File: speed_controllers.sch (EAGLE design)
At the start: 31 parts, among them M1 TE-1-1123723-3, M2 TE-1-1123723-3, M3 TE-1-1123723-3, M4 TE-1-1123723-3, M5 TE-1-1123723-3, M6 TE-1-1123723-3, M7 TE-1-1123723-3, M8 TE-1-1123723-3

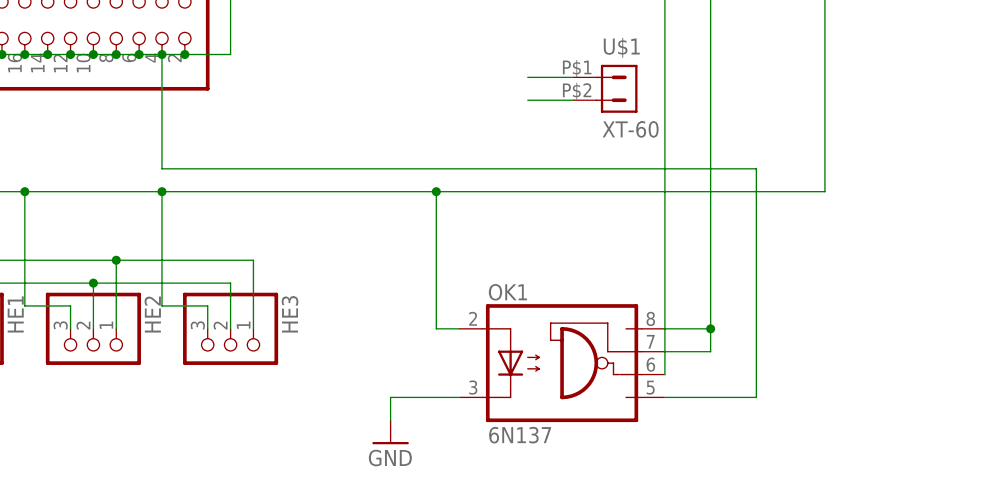
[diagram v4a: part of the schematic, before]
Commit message: Changed optocoupler to SMD
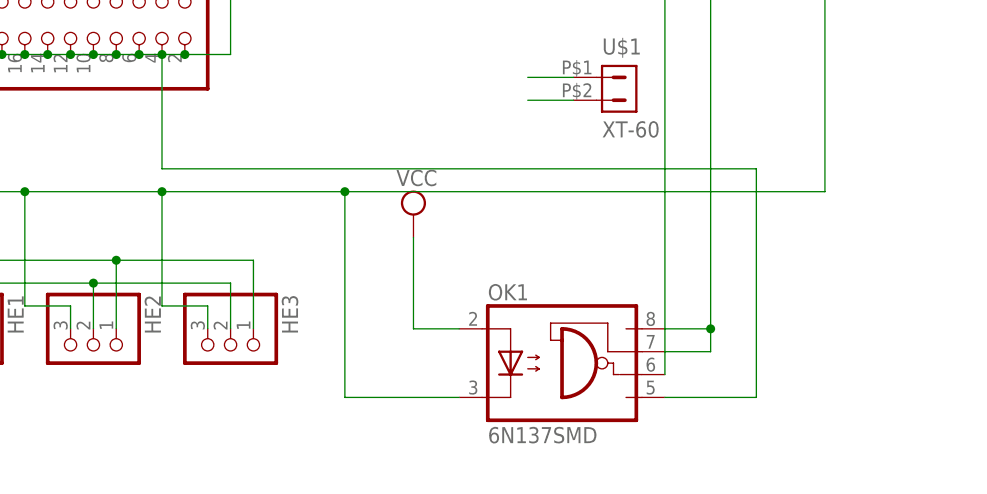
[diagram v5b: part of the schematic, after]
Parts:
- OK1: value 6N137 -> 6N137SMD; device auv:6N137 -> auv:6N137SMD
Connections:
- net FET_G: now also OK1.C; no longer OK1.A
- net GND: no longer OK1.C
- net VCC: now also OK1.A
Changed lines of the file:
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@@
 <part name="R1" library="auv" deviceset="R-US_" device="R0603"/>
 <part name="SUPPLY9" library="auv" deviceset="VCC" device=""/>
-<part name="OK1" library="auv" deviceset="6N137" device=""/>
-<part name="GND9" library="auv" deviceset="GND" device=""/>
 <part name="JP1" library="auv" deviceset="PINHD-2X10" device=""/>
+<part name="OK1" library="auv" deviceset="6N137" device="SMD"/>
+<part name="SUPPLY10" library="auv" deviceset="VCC" device=""/>
 </parts>
 <sheets>
@@
 <instance part="R1" gate="G$1" x="17.78" y="-86.36" rot="R90"/>
 <instance part="SUPPLY9" gate="G$1" x="12.7" y="-81.28" rot="R90"/>
+<instance part="JP1" gate="A" x="35.56" y="-71.12" rot="R270"/>
 <instance part="OK1" gate="A" x="88.9" y="-111.76"/>
-<instance part="GND9" gate="1" x="68.58" y="-119.38"/>
-<instance part="JP1" gate="A" x="35.56" y="-71.12" rot="R270"/>
+<instance part="SUPPLY10" gate="G$1" x="71.12" y="-93.98"/>
 </instances>
 <busses>
@@
 <junction x="35.56" y="-101.6"/>
 </segment>
-<segment>
-<pinref part="OK1" gate="A" pin="C"/>
-<pinref part="GND9" gate="1" pin="GND"/>
-<wire x1="76.2" y1="-114.3" x2="68.58" y2="-114.3" width="0.1524" layer="91"/>
-<wire x1="68.58" y1="-114.3" x2="68.58" y2="-116.84" width="0.1524" layer="91"/>
-</segment>
 </net>
 <net name="VCC" class="0">
@@
 <wire x1="17.78" y1="-81.28" x2="15.24" y2="-81.28" width="0.1524" layer="91"/>
 </segment>
+<segment>
+<pinref part="SUPPLY10" gate="G$1" pin="VCC"/>
+<wire x1="71.12" y1="-96.52" x2="71.12" y2="-106.68" width="0.1524" layer="91"/>
+<pinref part="OK1" gate="A" pin="A"/>
+<wire x1="76.2" y1="-106.68" x2="71.12" y2="-106.68" width="0.1524" layer="91"/>
+</segment>
 </net>
 <net name="FET_G" class="0">
@@
 <wire x1="116.84" y1="30.48" x2="116.84" y2="-30.48" width="0.1524" layer="91"/>
 <wire x1="116.84" y1="-30.48" x2="116.84" y2="-91.44" width="0.1524" layer="91"/>
-<wire x1="116.84" y1="-91.44" x2="73.66" y2="-91.44" width="0.1524" layer="91"/>
+<wire x1="116.84" y1="-91.44" x2="63.5" y2="-91.44" width="0.1524" layer="91"/>
 <pinref part="FET7" gate="G$1" pin="G"/>
-<wire x1="73.66" y1="-91.44" x2="43.18" y2="-91.44" width="0.1524" layer="91"/>
+<wire x1="63.5" y1="-91.44" x2="43.18" y2="-91.44" width="0.1524" layer="91"/>
 <wire x1="43.18" y1="-91.44" x2="27.94" y2="-91.44" width="0.1524" layer="91"/>
 <wire x1="27.94" y1="-91.44" x2="17.78" y2="-91.44" width="0.1524" layer="91"/>
@@
 <pinref part="R1" gate="G$1" pin="1"/>
 <junction x="17.78" y="-91.44"/>
-<pinref part="OK1" gate="A" pin="A"/>
-<wire x1="76.2" y1="-106.68" x2="73.66" y2="-106.68" width="0.1524" layer="91"/>
-<wire x1="73.66" y1="-106.68" x2="73.66" y2="-91.44" width="0.1524" layer="91"/>
-<junction x="73.66" y="-91.44"/>
+<pinref part="OK1" gate="A" pin="C"/>
+<wire x1="76.2" y1="-114.3" x2="63.5" y2="-114.3" width="0.1524" layer="91"/>
+<wire x1="63.5" y1="-114.3" x2="63.5" y2="-91.44" width="0.1524" layer="91"/>
+<junction x="63.5" y="-91.44"/>
 </segment>
 </net>
@@
 <wire x1="43.18" y1="-76.2" x2="43.18" y2="-88.9" width="0.1524" layer="91"/>
 <wire x1="43.18" y1="-88.9" x2="109.22" y2="-88.9" width="0.1524" layer="91"/>
-<pinref part="OK1" gate="A" pin="GND"/>
 <wire x1="109.22" y1="-88.9" x2="109.22" y2="-114.3" width="0.1524" layer="91"/>
 <wire x1="109.22" y1="-114.3" x2="99.06" y2="-114.3" width="0.1524" layer="91"/>
+<pinref part="OK1" gate="A" pin="GND"/>
 </segment>
 </net>
@@
 <net name="N$4" class="0">
 <segment>
-<pinref part="OK1" gate="A" pin="VE"/>
 <wire x1="99.06" y1="-109.22" x2="104.14" y2="-109.22" width="0.1524" layer="91"/>
-<pinref part="OK1" gate="A" pin="VCC"/>
 <wire x1="104.14" y1="-109.22" x2="104.14" y2="-106.68" width="0.1524" layer="91"/>
 <wire x1="104.14" y1="-106.68" x2="99.06" y2="-106.68" width="0.1524" layer="91"/>
@@
 <pinref part="JP1" gate="A" pin="1"/>
 <wire x1="45.72" y1="-63.5" x2="45.72" y2="-68.58" width="0.1524" layer="91"/>
+<pinref part="OK1" gate="A" pin="VCC"/>
+<pinref part="OK1" gate="A" pin="VE"/>
 </segment>
 </net>
 <net name="N$5" class="0">
 <segment>
-<pinref part="OK1" gate="A" pin="VO"/>
 <pinref part="JP1" gate="A" pin="3"/>
 <wire x1="99.06" y1="-111.76" x2="99.06" y2="-68.58" width="0.1524" layer="91"/>
 <wire x1="99.06" y1="-68.58" x2="43.18" y2="-68.58" width="0.1524" layer="91"/>
-</segment>
-</net>
+<pinref part="OK1" gate="A" pin="VO"/>
+</segment>
+</net>
